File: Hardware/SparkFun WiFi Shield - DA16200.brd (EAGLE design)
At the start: 59.7 x 53.3 mm, 139 parts, among them J1 CORTEX_JTAG_DEBUG, J2 QWIIC_RA, U1 DA16200MOD

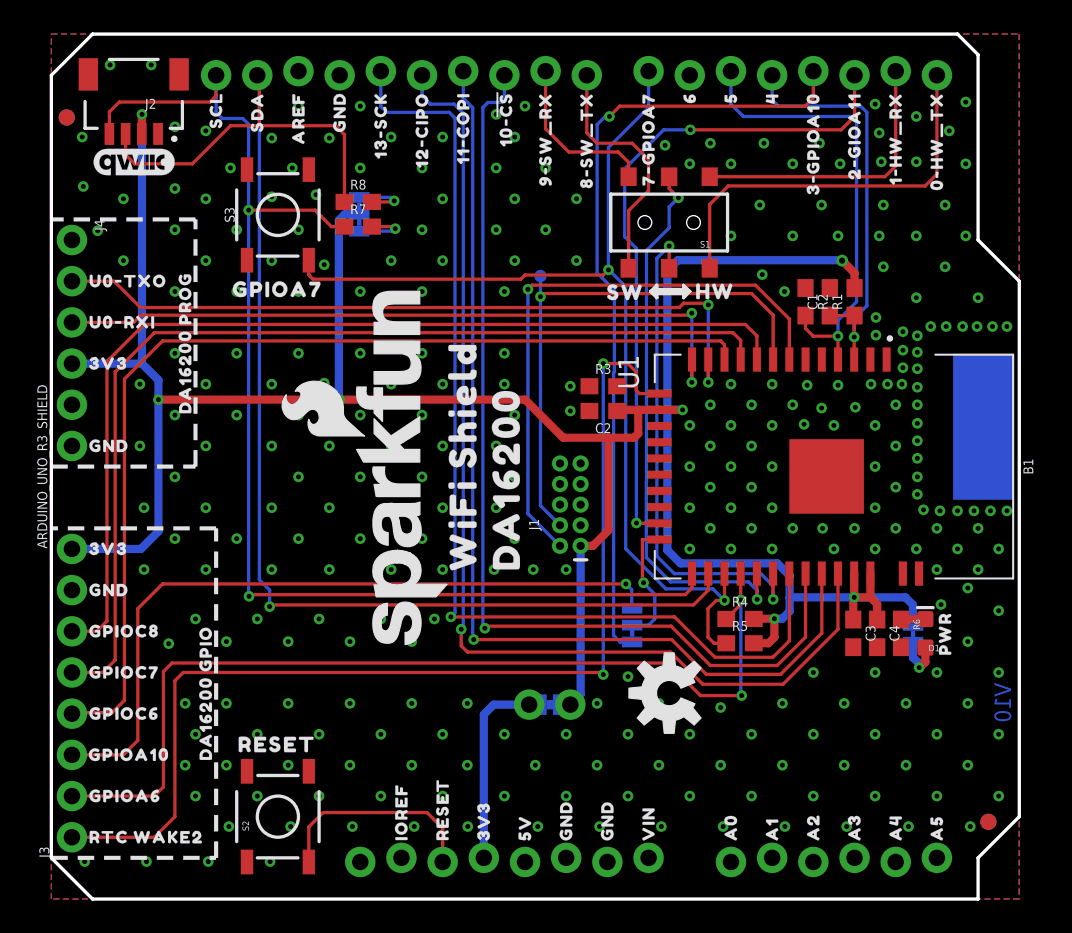
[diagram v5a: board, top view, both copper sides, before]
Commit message: Added jumpers for GPIOA0-3
Jumpers select between either SPI or GPIO/ADC functionality on the DA16200
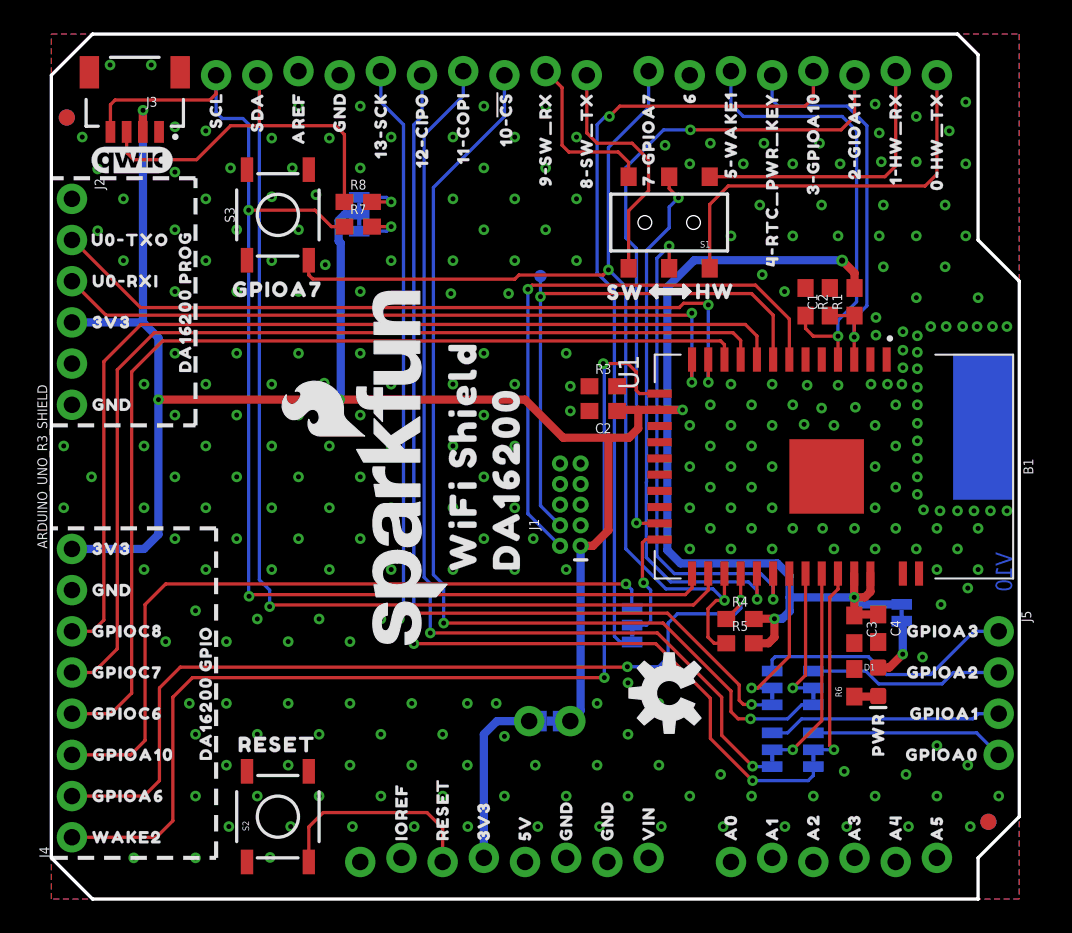
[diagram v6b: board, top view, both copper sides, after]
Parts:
- added J5: (no value), SparkFun-Connectors:1X04_NO_SILK
- added JP3, JP4, JP5, JP6: (no value), SparkFun-Jumpers:SMT-JUMPER_3_1-NC_TRACE_SILK
- added U$102, U$116: (no value), output:GPIOA20
- added U$103, U$117: (no value), output:GPIOA30
- added U$114, U$94: (no value), output:GPIOA10
- added U$115, U$93: (no value), output:GPIOA00
- added U$118, U$119, U$120, U$121: (no value), output:HEADER0
- added U$122: (no value), output:D100
- added U$123: (no value), output:D110
- added U$124: (no value), output:D120
- added U$125: (no value), output:D130
- J2: value QWIIC_RA -> (none); device SparkFun-Connectors:JST04_1MM_RA -> SparkFun-Connectors:1X06_NO_SILK
- J3: value (none) -> QWIIC_RA; device SparkFun-Connectors:1X08_NO_SILK -> SparkFun-Connectors:JST04_1MM_RA
- J4: device SparkFun-Connectors:1X06_NO_SILK -> SparkFun-Connectors:1X08_NO_SILK
- U$18: device output:40 -> output:4#RTC_PWR_KEY0
- U$23: device output:40 -> output:5#WAKE10
- U$33: device output:50 -> output:5#WAKE10
- U$35, U$48: device output:RTC_WAKE20 -> output:WAKE20
- U$70: device output:50 -> output:4#RTC_PWR_KEY0
- moved J3 43.7 mm to (5.14, 47.3), turned to 180 degrees
- moved J4 36.8 mm to (1.27, 3.81), turned to 90 degrees
- moved JP2 13.6 mm to (47.0, 9.21)
- moved U$69 9.46 mm to (43.8, 16.9)
- moved U$106 8.70 mm to (34.0, 17.9)
- moved U$99 7.47 mm to (51.0, 8.26)
- moved U$96 6.03 mm to (34.0, 15.9)
- moved J2 5.52 mm to (1.27, 43.2), turned to 270 degrees
- moved R6 4.20 mm to (49.5, 13.3), turned to 90 degrees
- moved U$98 4.19 mm to (30.7, 9.40)
- moved D1 4.17 mm to (51.0, 13.4), turned to 270 degrees
- moved U$37 2.55 mm to (1.97, 35.6)
- moved U$52 2.55 mm to (1.97, 30.5)
- moved U$54 2.55 mm to (1.97, 38.1)
- moved U$84 2.55 mm to (1.97, 38.1)
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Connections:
- removed net HEADER_GPIOA10: J3.3, JP2.1
- removed net HEADER_GPIOA6: J3.2, R4.1, U1.27
- removed net HEADER_GPIOC6: J3.4, U1.11
- removed net HEADER_GPIOC7: J3.5, U1.10
- removed net HEADER_GPIOC8: J3.6, U1.9
- removed net HEADER_RTC_WAKE2: J3.1, R3.2, U1.14
- removed net SPI_CLK: B1.D13, U1.30
- new net GPIOA0: JP2.2, U1.33
- new net GPIOA1: JP3.2, U1.32
- new net GPIOA2: JP4.2, U1.31
- new net GPIOA3: JP5.2, U1.30
- new net HDR_GPIOA0: J5.4, JP2.1
- new net HDR_GPIOA1: J5.3, JP3.1
- new net HDR_GPIOA10: J4.3, JP6.1
- new net HDR_GPIOA2: J5.2, JP4.1
- new net HDR_GPIOA3: J5.1, JP5.1
- new net HDR_GPIOA6: J4.2, R4.1, U1.27
- new net HDR_GPIOC6: J4.4, U1.11
- new net HDR_GPIOC7: J4.5, U1.10
- new net HDR_GPIOC8: J4.6, U1.9
- new net HDR_RTC_WAKE2: J4.1, R3.2, U1.14
- new net SPI_SCK: B1.D13, JP5.3
- net 3.3V: now also J2.4, J3.2, J4.8; no longer J2.2, J3.8, J4.4
- net ARD_GPIOA10: now also JP6.3; no longer JP2.3
- net ARD_SCL: now also J3.4; no longer J2.4
- net ARD_SDA: now also J3.3; no longer J2.3
- net GND: now also J2.6, J3.1, J4.7; no longer J2.1, J3.7, J4.6
- net GPIOA10: now also JP6.2; no longer JP2.2
- net SPI_CIPO: now also JP2.3; no longer U1.33
- net SPI_COPI: now also JP3.3; no longer U1.32
- net SPI_CS: now also JP4.3; no longer U1.31
- net U0RXI: now also J2.3; no longer J4.3
- net U0TXO: now also J2.2; no longer J4.2
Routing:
- net HEADER_RTC_WAKE2: track 67.2 -> 0.00 mm, vias 2 -> 0
- net HDR_RTC_WAKE2: track 0.00 -> 66.9 mm, vias 0 -> 2
- net SPI_CLK: track 64.4 -> 0.00 mm, vias 1 -> 0
- net HEADER_GPIOC6: track 62.4 -> 0.00 mm
- net HDR_GPIOC6: track 0.00 -> 62.4 mm
- net HEADER_GPIOC7: track 61.7 -> 0.00 mm
- net HDR_GPIOC7: track 0.00 -> 61.4 mm
- net HEADER_GPIOC8: track 61.2 -> 0.00 mm
- net HDR_GPIOC8: track 0.00 -> 61.2 mm
- net SPI_SCK: track 0.00 -> 60.5 mm, vias 0 -> 2
- net HEADER_GPIOA6: track 58.8 -> 0.00 mm, vias 2 -> 0
- net HDR_GPIOA6: track 0.00 -> 54.3 mm, vias 0 -> 2
- net HDR_GPIOA10: track 0.00 -> 45.1 mm, vias 0 -> 1
- net HEADER_GPIOA10: track 44.9 -> 0.00 mm, vias 1 -> 0
- net HDR_GPIOA3: track 0.00 -> 16.3 mm
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
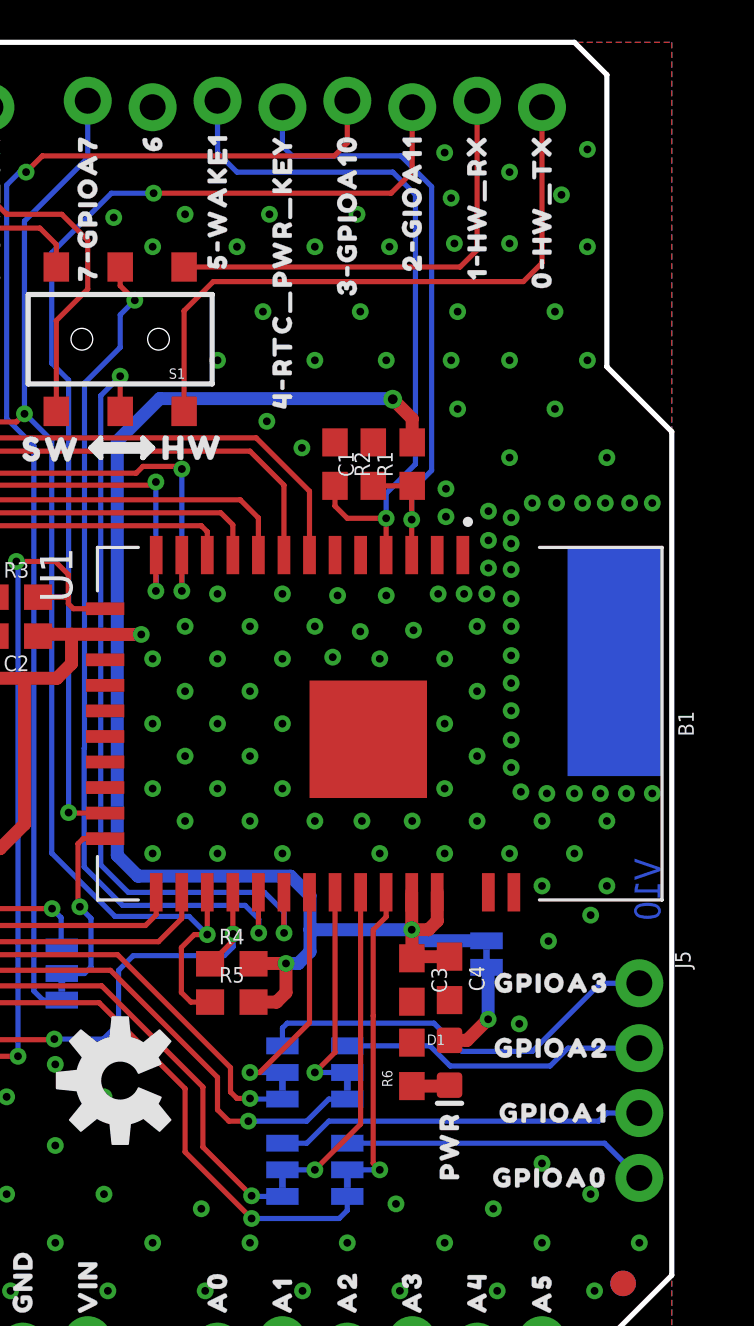
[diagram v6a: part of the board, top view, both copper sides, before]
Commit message: Update SparkFun WiFi Shield - DA16200.brd
Updated vias
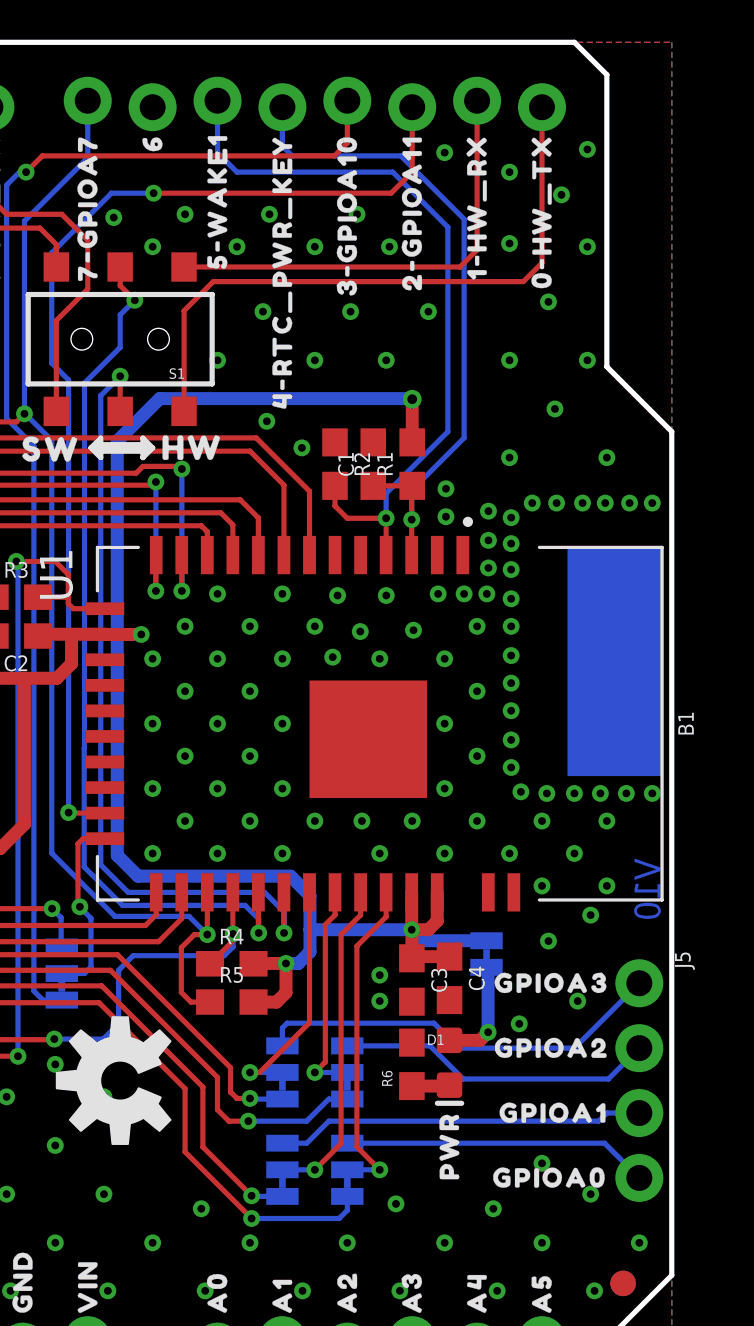
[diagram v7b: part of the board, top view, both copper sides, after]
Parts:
- removed U$22, U$67: (no value), output:2#GIOA110
- added U$109, U$50: (no value), output:2#GPIOA110
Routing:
- net RTC_WAKE1: track 28.0 -> 29.1 mm
- net RTC_PWR_KEY: track 25.6 -> 26.7 mm
- net GPIOA0: track 12.4 -> 13.0 mm
